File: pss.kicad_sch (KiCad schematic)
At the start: 33 parts, among them J101 Conn_01x06_Socket, J102 Conn_01x02_Socket, J103 Conn_01x02_Socket, J104 Conn_01x02_Socket

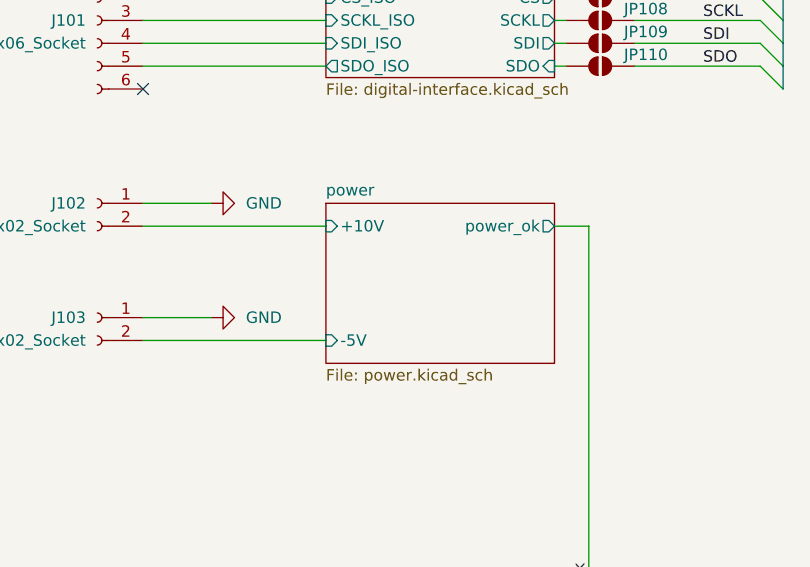
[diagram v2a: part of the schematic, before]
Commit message: fix schematic netlist error, two nets with same name
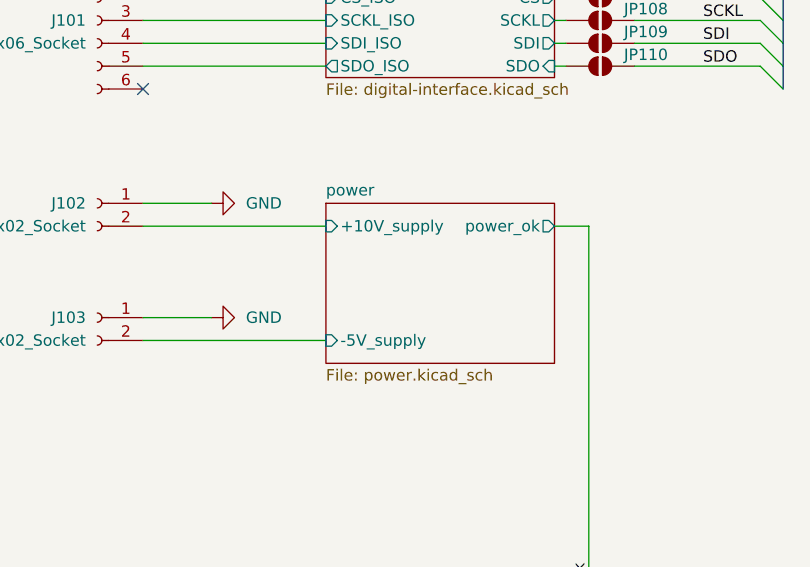
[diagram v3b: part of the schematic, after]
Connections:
- net power/+10V renamed power/+10V_supply
- net power/-5V renamed power/-5V_supply
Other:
- sheet power ports: added +10V_supply, -5V_supply; removed +10V, -5V
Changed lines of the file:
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@@
 		(title "Power Supply Sink")
 		(date "2024-12-08")
-		(rev "0.13.5")
+		(rev "0.13.6")
 		(company "Open Battery Tester")
 		(comment 1 "Overview")
@@
 			)
 		)
-		(pin "+10V" input
-			(at 63.5 53.34 180)
+		(pin "-5V_supply" input
+			(at 63.5 66.04 180)
 			(effects
 				(font
@@
 			)
 		)
-		(pin "-5V" input
-			(at 63.5 66.04 180)
+		(pin "+10V_supply" input
+			(at 63.5 53.34 180)
 			(effects
 				(font

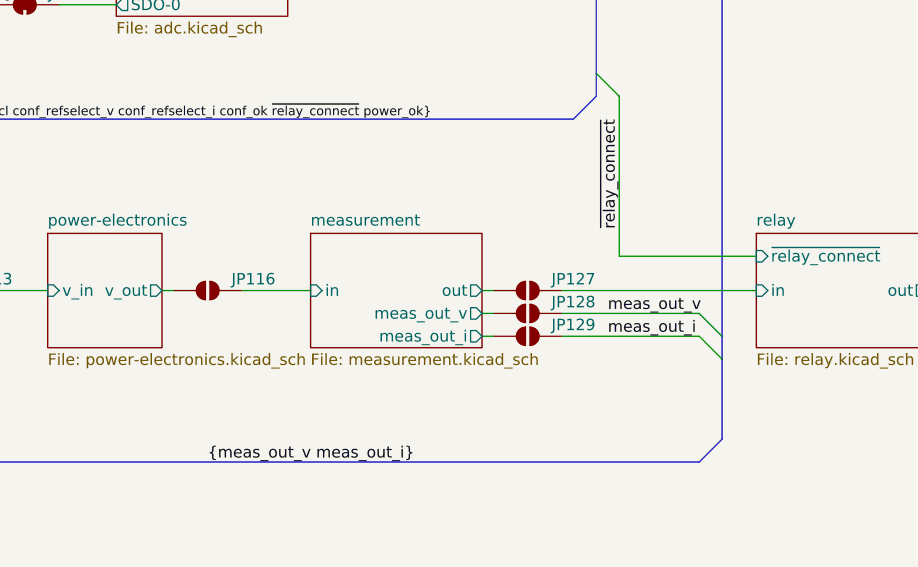
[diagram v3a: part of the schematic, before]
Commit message: remove pss solder jumper in output current flow around measurement sub circuit
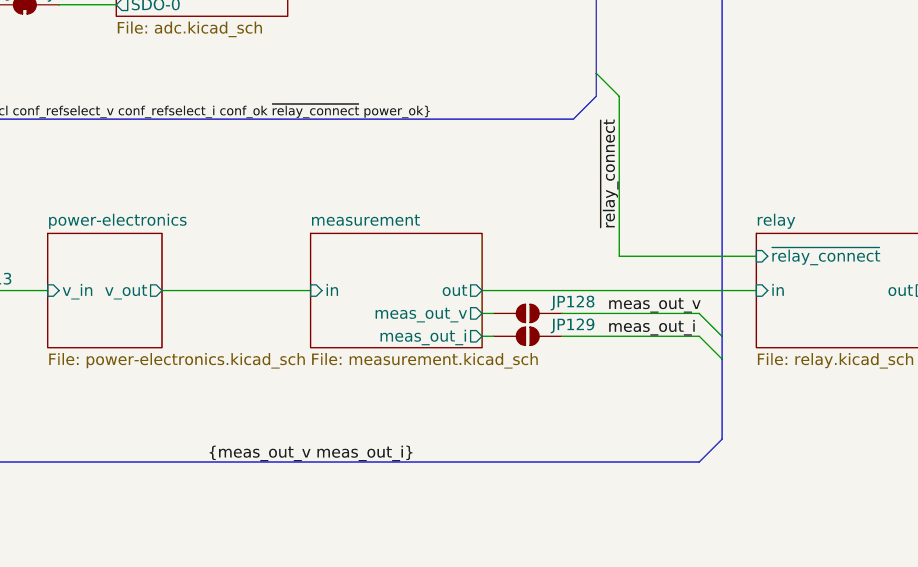
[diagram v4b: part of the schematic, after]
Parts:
- removed JP116, JP127: SolderJumper_2_Open, pss:SolderJumper-2_P1.3mm_Open_RoundedPad1.0x1.5mm, symbol pss:SolderJumper_2_Open
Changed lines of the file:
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@@
 	(title_block
 		(title "Power Supply Sink")
-		(date "2024-12-08")
-		(rev "0.13.6")
+		(date "2024-12-09")
+		(rev "0.13.7")
 		(company "Open Battery Tester")
 		(comment 1 "Overview")
@@
 	(wire
 		(pts
-			(xy 185.42 120.65) (xy 186.69 120.65)
+			(xy 185.42 120.65) (xy 215.9 120.65)
 		)
 		(stroke
@@
 	(wire
 		(pts
-			(xy 158.75 120.65) (xy 166.37 120.65)
-		)
-		(stroke
-			(width 0)
-			(type default)
-		)
-	)
-	(wire
-		(pts
 			(xy 200.66 116.84) (xy 215.9 116.84)
 		)
@@
 	(wire
 		(pts
-			(xy 194.31 120.65) (xy 215.9 120.65)
-		)
-		(stroke
-			(width 0)
-			(type default)
-		)
-	)
-	(wire
-		(pts
 			(xy 68.58 130.81) (xy 68.58 140.97)
 		)
@@
 	(wire
 		(pts
-			(xy 149.86 120.65) (xy 151.13 120.65)
+			(xy 149.86 120.65) (xy 166.37 120.65)
 		)
 		(stroke
@@
 		(length 2.54)
 		(shape diamond)
-		(at 186.69 120.65 0)
-		(fields_autoplaced yes)
-		(effects
-			(font
-				(size 1.27 1.27)
-			)
-			(justify left bottom)
-		)
-		(property "Netclass" "25A"
-			(at 187.8965 118.11 0)
-			(effects
-				(font
-					(size 1.27 1.27)
-					(italic yes)
-				)
-				(justify left)
-			)
-		)
-	)
-	(netclass_flag ""
-		(length 2.54)
-		(shape diamond)
 		(at 44.45 50.8 0)
 		(fields_autoplaced yes)
@@
 		(length 2.54)
 		(shape diamond)
-		(at 151.13 120.65 180)
-		(fields_autoplaced yes)
-		(effects
-			(font
-				(size 1.27 1.27)
-			)
-			(justify right bottom)
-		)
-		(property "Netclass" "25A"
-			(at 152.3365 123.19 0)
-			(effects
-				(font
-					(size 1.27 1.27)
-					(italic yes)
-				)
-				(justify left)
-			)
-		)
-	)
-	(netclass_flag ""
-		(length 2.54)
-		(shape diamond)
 		(at 248.92 118.11 0)
 		(fields_autoplaced yes)
@@
 	(symbol
 		(lib_id "pss:SolderJumper_2_Open")
-		(at 154.94 120.65 0)
-		(unit 1)
-		(exclude_from_sim yes)
-		(in_bom no)
-		(on_board yes)
-		(dnp no)
-		(property "Reference" "JP116"
-			(at 160.02 119.38 0)
-			(effects
-				(font
-					(size 1.27 1.27)
-				)
-			)
-		)
-		(property "Value" "SolderJumper_2_Open"
-			(at 129.54 107.95 0)
-			(effects
-				(font
-					(size 1.27 1.27)
-				)
-				(hide yes)
-			)
-		)
-		(property "Footprint" "pss:SolderJumper-2_P1.3mm_Open_RoundedPad1.0x1.5mm"
-			(at 154.94 120.65 0)
-			(effects
-				(font
-					(size 1.27 1.27)
-				)
-				(hide yes)
-			)
-		)
-		(property "Datasheet" "~"
-			(at 154.94 120.65 0)
-			(effects
-				(font
-					(size 1.27 1.27)
-				)
-				(hide yes)
-			)
-		)
-		(property "Description" "Solder Jumper, 2-pole, open"
-			(at 154.94 120.65 0)
-			(effects
-				(font
-					(size 1.27 1.27)
-				)
-				(hide yes)
-			)
-		)
-		(pin "1"
-		)
-		(pin "2"
-		)
-		(instances
-			(project "pss"
-				(path "/3c438cf7-9350-4e9f-8115-1deba8984176"
-					(reference "JP116")
-					(unit 1)
-				)
-			)
-		)
-	)
-	(symbol
-		(lib_id "pss:SolderJumper_2_Open")
 		(at 125.73 120.65 0)
 		(unit 1)
@@
 					(unit 1)
 				)
-			)
-		)
-	)
-	(symbol
-		(lib_id "pss:SolderJumper_2_Open")
-		(at 190.5 120.65 0)
-		(unit 1)
-		(exclude_from_sim yes)
-		(in_bom no)
-		(on_board yes)
-		(dnp no)
-		(property "Reference" "JP127"
-			(at 195.58 119.38 0)
-			(effects
-				(font
-					(size 1.27 1.27)
-				)
-			)
-		)
-		(property "Value" "SolderJumper_2_Open"
-			(at 165.1 107.95 0)
-			(effects
-				(font
-					(size 1.27 1.27)
-				)
-				(hide yes)
-			)
-		)
-		(property "Footprint" "pss:SolderJumper-2_P1.3mm_Open_RoundedPad1.0x1.5mm"
-			(at 190.5 120.65 0)
-			(effects
-				(font
-					(size 1.27 1.27)
-				)
-				(hide yes)
-			)
-		)
-		(property "Datasheet" "~"
-			(at 190.5 120.65 0)
-			(effects
-				(font
-					(size 1.27 1.27)
-				)
-				(hide yes)
-			)
-		)
-		(property "Description" "Solder Jumper, 2-pole, open"
-			(at 190.5 120.65 0)
-			(effects
-				(font
-					(size 1.27 1.27)
-				)
-				(hide yes)
-			)
-		)
-		(pin "1"
-		)
-		(pin "2"
-		)
-		(instances
-			(project "pss"
-				(path "/3c438cf7-9350-4e9f-8115-1deba8984176"
-					(reference "JP127")
-					(unit 1)
-				)
